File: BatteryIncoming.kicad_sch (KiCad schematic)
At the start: 8 parts, among them J2 DC Barrel Jack w/ Switch, K1 Relay_SPST-NO, SW1 Start, SW2 Stop, SW3 E-Stop

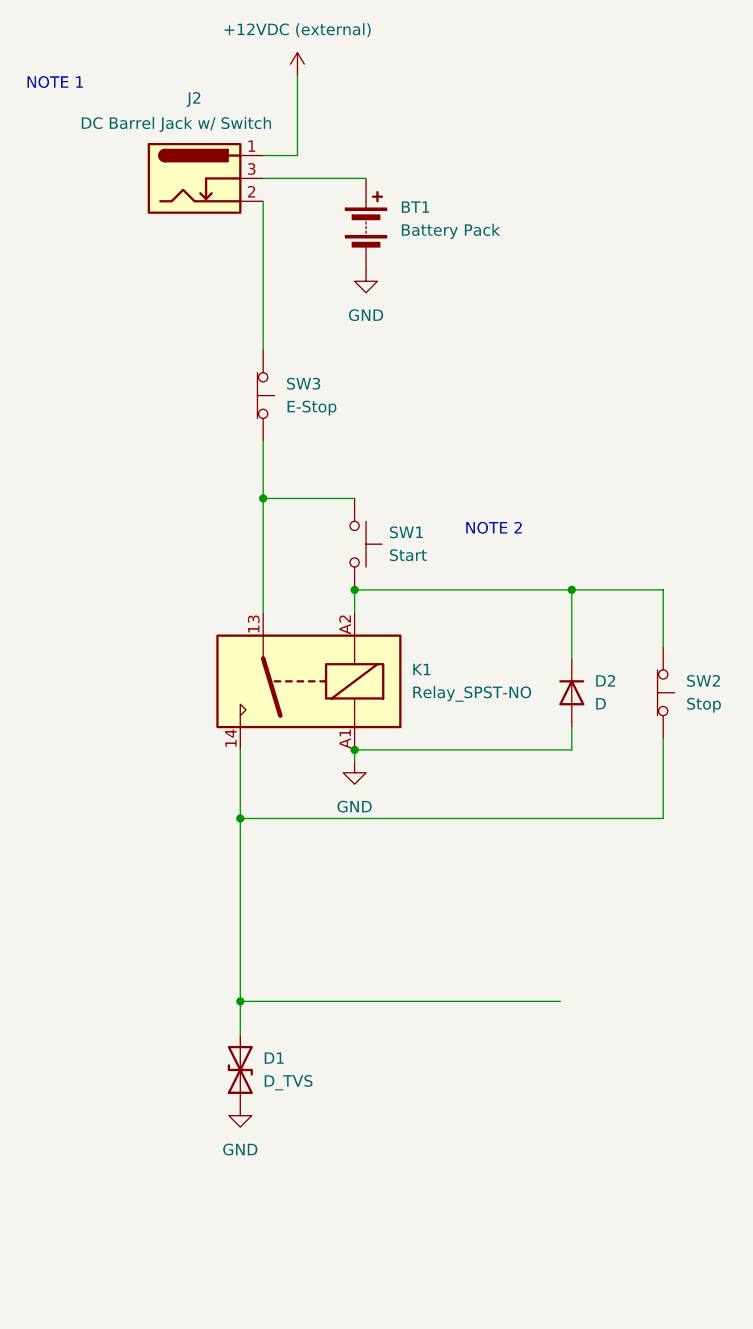
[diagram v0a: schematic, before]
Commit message: - Added reverse polarity PMOS protection circuit.
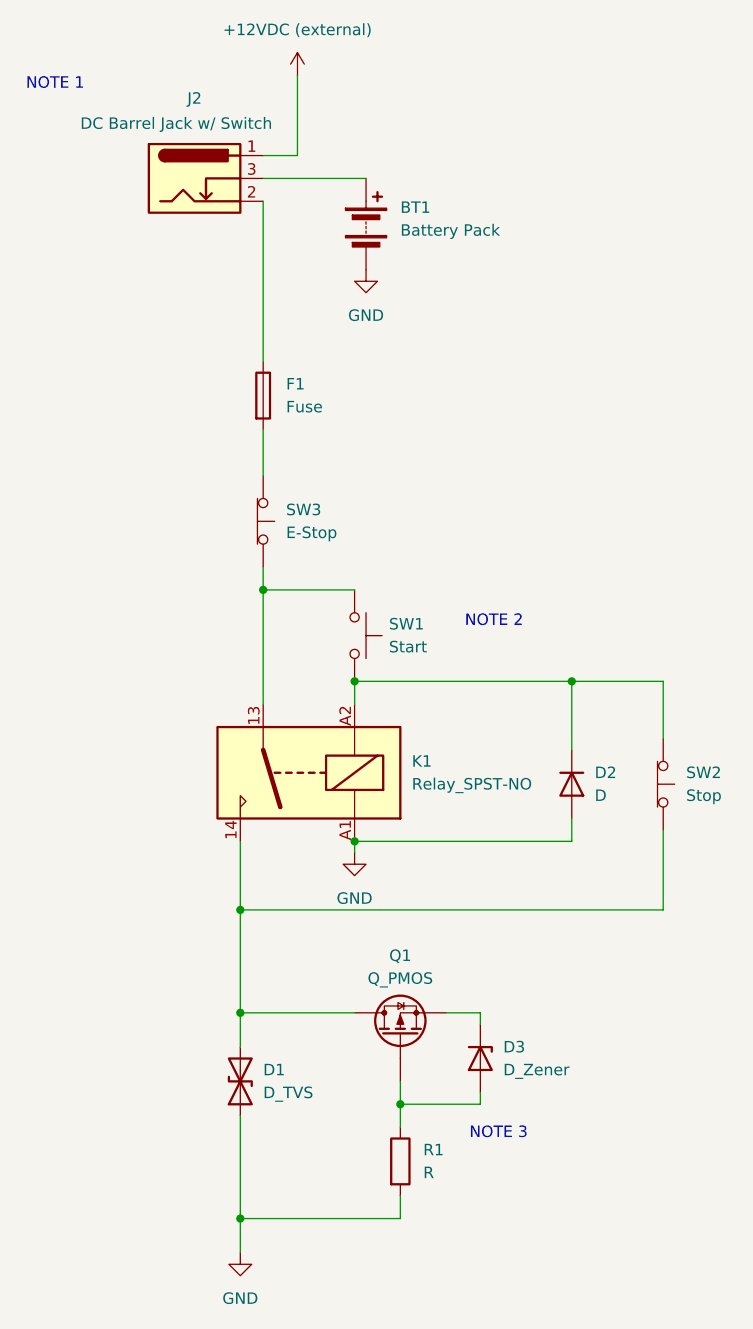
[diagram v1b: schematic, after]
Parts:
- added D3: D_Zener, symbol Device:D_Zener
- added F1: Fuse, symbol Device:Fuse
- added Q1: Q_PMOS, symbol Device:Q_PMOS
- added R1: R, symbol Device:R
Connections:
- net GND: now also R1.2
- net at D1.2 (A2), K1.14, SW2.2 (B): now also Q1.D
- net at J2.2: now also F1.1; no longer SW3.1 (A)
- new net: D3.2 (A), Q1.G, R1.1
- new net: D3.1 (K), Q1.S
- new net: F1.2, SW3.1 (A)
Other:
- note added: "NOTE 3"
- moved on the sheet: D1, D2, K1, SW1, SW2, SW3
